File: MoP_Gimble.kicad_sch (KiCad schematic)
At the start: 17 parts, among them J1 Servo1, J5 Conn_01x02, J6 Conn_01x02, J7 Servo2, U10 74LVC2G14, U3 L293D, U9 74LVC2G14

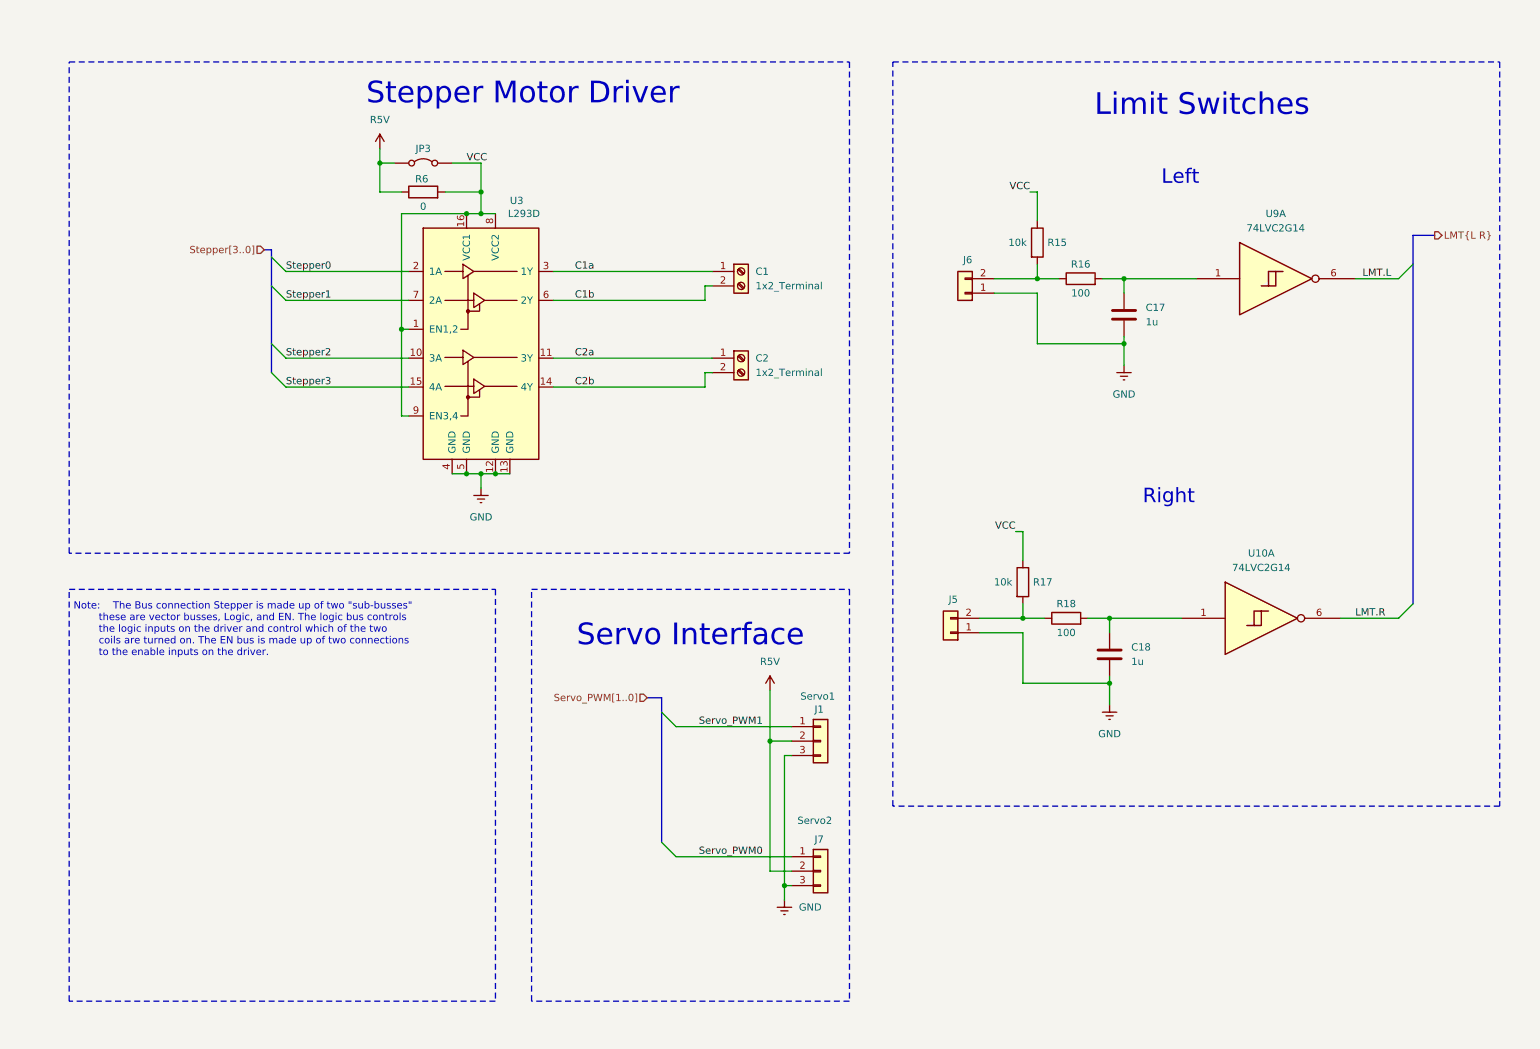
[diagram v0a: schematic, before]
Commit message: changed ref designators to be consistent accross sheets
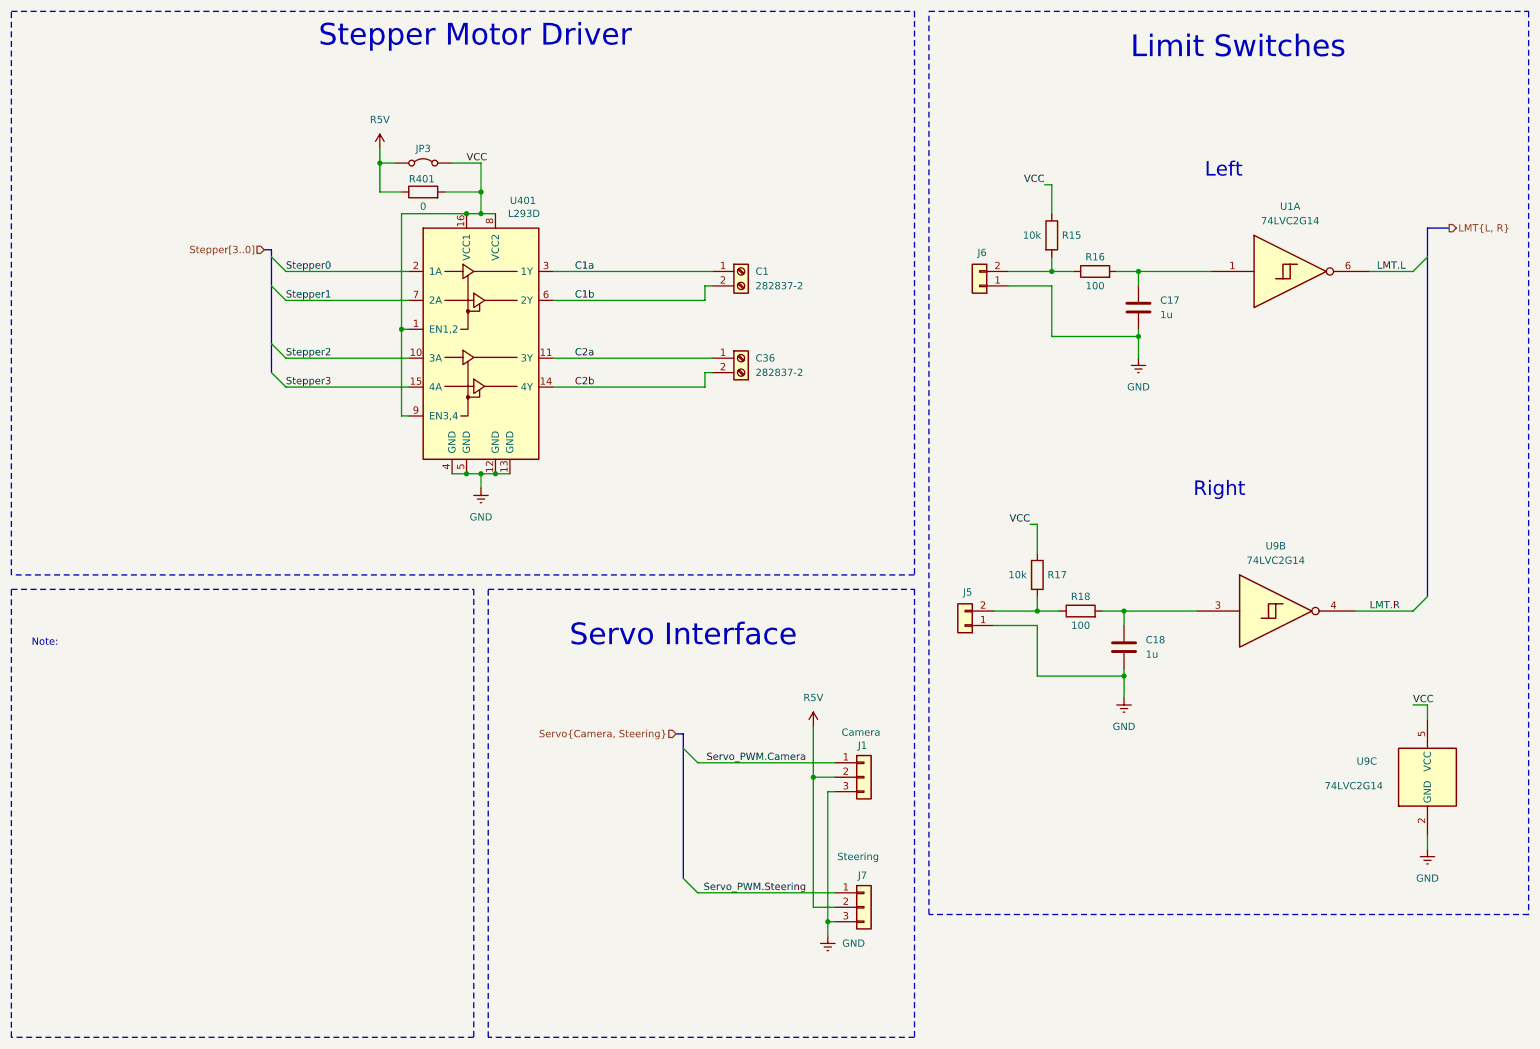
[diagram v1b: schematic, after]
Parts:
- removed C2: 1x2_Terminal, symbol Connector:Screw_Terminal_01x02
- added C36: 282837-2, TerminalBlock_Phoenix:TerminalBlock_Phoenix_MKDS-1,5-2-5.08_1x02_P5.08mm_Horizontal, symbol Connector:Screw_Terminal_01x02
- added U1: 74LVC2G14, symbol 74xGxx:74LVC2G14
- C1: value 1x2_Terminal -> 282837-2; footprint (none) -> TerminalBlock_Phoenix:TerminalBlock_Phoenix_MKDS-1,5-2-5.08_1x02_P5.08mm_Horizontal
- J1: value Servo1 -> Camera
- J7: value Servo2 -> Steering
- U401: renamed from U3; footprint Package_DIP:DIP-20_W7.62mm_SMDSocket_SmallPads -> Package_DIP:DIP-16_W7.62mm_LongPads
- renumbered R6 to R401, U10 to U9
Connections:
- net C2a: now also C36.1 (Pin_1)
- net C2b: now also C36.2 (Pin_2)
- net GND: now also U9.2 (GND)
- net LMT.L: now also U1.6; no longer U9.6
- net LMT.R: now also U9.4; no longer U9.6
- net VCC: now also U9.5 (VCC)
- net at C17.1, R16.2: now also U1.1; no longer U9.1
- net at C18.1, R18.2: now also U9.3; no longer U9.1
- net Servo_PWM0 renamed Servo_PWM.Steering
- net Servo_PWM1 renamed Servo_PWM.Camera
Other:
- note added: "Note:"
- note removed: "Note: The Bus connection Stepper is made up of two "sub-busses" these are vector busses, Logic, and EN. The logic bus controls the logic inputs on the driver and control which of the two coils are turned on. The EN bus is made up of two connections to the enable inputs on the driver."
- moved on the sheet: C17, C18, J1, J5, J6, J7, R15, R16, R17, R18, U9B

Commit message: Finished schematics
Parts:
- C402: renamed from C18; footprint (none) -> Capacitor_SMD:C_0805_2012Metric_Pad1.18x1.45mm_HandSolder
- J404: renamed from J1; footprint (none) -> Connector_PinHeader_2.54mm:PinHeader_1x02_P2.54mm_Vertical
- JP3: footprint (none) -> Connector_PinHeader_2.54mm:PinHeader_1x02_P2.54mm_Vertical
- R401: footprint (none) -> Resistor_SMD:R_0805_2012Metric; now not fitted
- R402: renamed from R15; footprint (none) -> Resistor_SMD:R_0805_2012Metric
- R403: renamed from R16; footprint (none) -> Resistor_SMD:R_0805_2012Metric
- R404: renamed from R17; footprint (none) -> Resistor_SMD:R_0805_2012Metric
- R405: renamed from R18; footprint (none) -> Resistor_SMD:R_0805_2012Metric
- U401: footprint Package_DIP:DIP-16_W7.62mm_LongPads -> Package_SO:SO-20_12.8x7.5mm_P1.27mm
- U402: renamed from U9; footprint (none) -> Package_TO_SOT_SMD:SOT-23-6
- U402: renamed from U1; footprint (none) -> Package_TO_SOT_SMD:SOT-23-6
- renumbered C17 to C401, J6 to J401, C1 to J402, C36 to J403, J7 to J405, J5 to J405
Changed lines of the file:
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@@
 		(on_board yes)
 		(dnp no)
-		(property "Reference" "U9"
+		(property "Reference" "U402"
 			(at 253.492 147.066 0)
 			(effects
@@
 			)
 		)
-		(property "Footprint" ""
+		(property "Footprint" "Package_TO_SOT_SMD:SOT-23-6"
 			(at 264.16 149.86 0)
 			(effects
@@
 			(project ""
 				(path "/4d76798e-9a11-4d8d-a723-72f274a89091/ae2123db-e8af-4be5-b4d9-fa1dc199daa4"
-					(reference "U9")
+					(reference "U402")
 					(unit 3)
 				)
@@
 		(dnp no)
 		(fields_autoplaced yes)
-		(property "Reference" "C17"
+		(property "Reference" "C401"
 			(at 217.17 66.0399 0)
 			(effects
@@
 			(project ""
 				(path "/4d76798e-9a11-4d8d-a723-72f274a89091/ae2123db-e8af-4be5-b4d9-fa1dc199daa4"
-					(reference "C17")
+					(reference "C401")
 					(unit 1)
 				)
@@
 		(on_board yes)
 		(dnp no)
-		(property "Reference" "R15"
+		(property "Reference" "R402"
 			(at 199.898 54.61 0)
 			(effects
@@
 			)
 		)
-		(property "Footprint" ""
+		(property "Footprint" "Resistor_SMD:R_0805_2012Metric"
 			(at 196.342 54.61 90)
 			(effects
@@
 			(project ""
 				(path "/4d76798e-9a11-4d8d-a723-72f274a89091/ae2123db-e8af-4be5-b4d9-fa1dc199daa4"
-					(reference "R15")
+					(reference "R402")
 					(unit 1)
 				)
@@
 		(dnp no)
 		(fields_autoplaced yes)
-		(property "Reference" "U1"
+		(property "Reference" "U402"
 			(at 240.03 49.53 0)
 			(effects
@@
 			)
 		)
-		(property "Footprint" ""
+		(property "Footprint" "Package_TO_SOT_SMD:SOT-23-6"
 			(at 241.3 60.96 0)
 			(effects
@@
 			(project "MoP"
 				(path "/4d76798e-9a11-4d8d-a723-72f274a89091/ae2123db-e8af-4be5-b4d9-fa1dc199daa4"
-					(reference "U1")
+					(reference "U402")
 					(unit 1)
 				)
@@
 		(dnp no)
 		(fields_autoplaced yes)
-		(property "Reference" "U9"
+		(property "Reference" "U402"
 			(at 237.49 109.22 0)
 			(effects
@@
 			)
 		)
-		(property "Footprint" ""
+		(property "Footprint" "Package_TO_SOT_SMD:SOT-23-6"
 			(at 238.76 120.65 0)
 			(effects
@@
 			(project "MoP"
 				(path "/4d76798e-9a11-4d8d-a723-72f274a89091/ae2123db-e8af-4be5-b4d9-fa1dc199daa4"
-					(reference "U9")
+					(reference "U402")
 					(unit 2)
 				)
@@
 		(on_board yes)
 		(dnp no)
-		(property "Reference" "J7"
+		(property "Reference" "J405"
 			(at 164.846 167.132 0)
 			(effects
@@
 			(project "MoP"
 				(path "/4d76798e-9a11-4d8d-a723-72f274a89091/ae2123db-e8af-4be5-b4d9-fa1dc199daa4"
-					(reference "J7")
+					(reference "J405")
 					(unit 1)
 				)
@@
 		(dnp no)
 		(fields_autoplaced yes)
-		(property "Reference" "C36"
+		(property "Reference" "J403"
 			(at 146.05 76.1999 0)
 			(effects
@@
 			(project "MoP"
 				(path "/4d76798e-9a11-4d8d-a723-72f274a89091/ae2123db-e8af-4be5-b4d9-fa1dc199daa4"
-					(reference "C36")
+					(reference "J403")
 					(unit 1)
 				)
@@
 		(dnp no)
 		(fields_autoplaced yes)
-		(property "Reference" "C18"
+		(property "Reference" "C402"
 			(at 214.63 125.7299 0)
 			(effects
@@
 			)
 		)
-		(property "Footprint" ""
+		(property "Footprint" "Capacitor_SMD:C_0805_2012Metric_Pad1.18x1.45mm_HandSolder"
 			(at 211.7852 130.81 0)
 			(effects
@@
 			(project "MoP"
 				(path "/4d76798e-9a11-4d8d-a723-72f274a89091/ae2123db-e8af-4be5-b4d9-fa1dc199daa4"
-					(reference "C18")
+					(reference "C402")
 					(unit 1)
 				)
@@
 		(on_board yes)
 		(dnp no)
-		(property "Reference" "J1"
+		(property "Reference" "J404"
 			(at 164.846 144.272 0)
 			(effects
@@
 			)
 		)
-		(property "Footprint" ""
+		(property "Footprint" "Connector_PinHeader_2.54mm:PinHeader_1x02_P2.54mm_Vertical"
 			(at 165.1 149.86 0)
 			(effects
@@
 			(project "MoP"
 				(path "/4d76798e-9a11-4d8d-a723-72f274a89091/ae2123db-e8af-4be5-b4d9-fa1dc199daa4"
-					(reference "J1")
+					(reference "J404")
 					(unit 1)
 				)
@@
 			)
 		)
-		(property "Footprint" "Package_DIP:DIP-16_W7.62mm_LongPads"
+		(property "Footprint" "Package_SO:SO-20_12.8x7.5mm_P1.27mm"
 			(at 104.14 95.25 0)
 			(effects
@@
 		(on_board yes)
 		(dnp no)
-		(property "Reference" "R17"
+		(property "Reference" "R404"
 			(at 197.358 114.3 0)
 			(effects
@@
 			)
 		)
-		(property "Footprint" ""
+		(property "Footprint" "Resistor_SMD:R_0805_2012Metric"
 			(at 193.802 114.3 90)
 			(effects
@@
 			(project "MoP"
 				(path "/4d76798e-9a11-4d8d-a723-72f274a89091/ae2123db-e8af-4be5-b4d9-fa1dc199daa4"
-					(reference "R17")
+					(reference "R404")
 					(unit 1)
 				)
@@
 		(on_board yes)
 		(dnp no)
-		(property "Reference" "J6"
+		(property "Reference" "J401"
 			(at 186.69 57.658 0)
 			(effects
@@
 			(project "MoP"
 				(path "/4d76798e-9a11-4d8d-a723-72f274a89091/ae2123db-e8af-4be5-b4d9-fa1dc199daa4"
-					(reference "J6")
+					(reference "J401")
 					(unit 1)
 				)
@@
 		(on_board yes)
 		(dnp no)
-		(property "Reference" "R16"
+		(property "Reference" "R403"
 			(at 205.74 58.42 90)
 			(effects
@@
 			)
 		)
-		(property "Footprint" ""
+		(property "Footprint" "Resistor_SMD:R_0805_2012Metric"
 			(at 205.74 62.738 90)
 			(effects
@@
 			(project "MoP"
 				(path "/4d76798e-9a11-4d8d-a723-72f274a89091/ae2123db-e8af-4be5-b4d9-fa1dc199daa4"
-					(reference "R16")
+					(reference "R403")
 					(unit 1)
 				)
@@
 		(dnp no)
 		(fields_autoplaced yes)
-		(property "Reference" "C1"
+		(property "Reference" "J402"
 			(at 146.05 60.9599 0)
 			(effects
@@
 			(project "MoP"
 				(path "/4d76798e-9a11-4d8d-a723-72f274a89091/ae2123db-e8af-4be5-b4d9-fa1dc199daa4"
-					(reference "C1")
+					(reference "J402")
 					(unit 1)
 				)
@@
 		(on_board yes)
 		(dnp no)
-		(property "Reference" "R18"
+		(property "Reference" "R405"
 			(at 203.2 118.11 90)
 			(effects
@@
 			)
 		)
-		(property "Footprint" ""
+		(property "Footprint" "Resistor_SMD:R_0805_2012Metric"
 			(at 203.2 122.428 90)
 			(effects
@@
 			(project "MoP"
 				(path "/4d76798e-9a11-4d8d-a723-72f274a89091/ae2123db-e8af-4be5-b4d9-fa1dc199daa4"
-					(reference "R18")
+					(reference "R405")
 					(unit 1)
 				)
@@
 		(exclude_from_sim no)
 		(in_bom yes)
-		(on_board yes)
-		(dnp no)
+		(on_board no)
+		(dnp yes)
 		(property "Reference" "R401"
 			(at 87.376 44.704 90)
@@
 			)
 		)
-		(property "Footprint" ""
+		(property "Footprint" "Resistor_SMD:R_0805_2012Metric"
 			(at 87.63 48.768 90)
 			(effects
@@
 			)
 		)
-		(property "Footprint" ""
+		(property "Footprint" "Connector_PinHeader_2.54mm:PinHeader_1x02_P2.54mm_Vertical"
 			(at 87.63 41.91 0)
 			(effects
@@
 		(on_board yes)
 		(dnp no)
-		(property "Reference" "J5"
+		(property "Reference" "J405"
 			(at 184.15 117.348 0)
 			(effects
@@
 			(project "MoP"
 				(path "/4d76798e-9a11-4d8d-a723-72f274a89091/ae2123db-e8af-4be5-b4d9-fa1dc199daa4"
-					(reference "J5")
-					(unit 1)
-				)
+					(reference "J405")
+					(unit 1)
+				)
